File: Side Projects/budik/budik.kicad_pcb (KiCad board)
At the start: 2 copper layers, 122 x 65 mm, 92 parts, among them J1 Conn_01x02_Male, J2 USB_OTG, J3 FTDI, Q1 BSS138, SW1 SW_DPST, SW2 SW_DPST, SW3 SW_SPDT, SW4 SW_DPST, SW5 SW_DPST, U1 ESP-12, U2 MCP23018-E_SP, U3 uA7805, U4 LD1117S33CTR

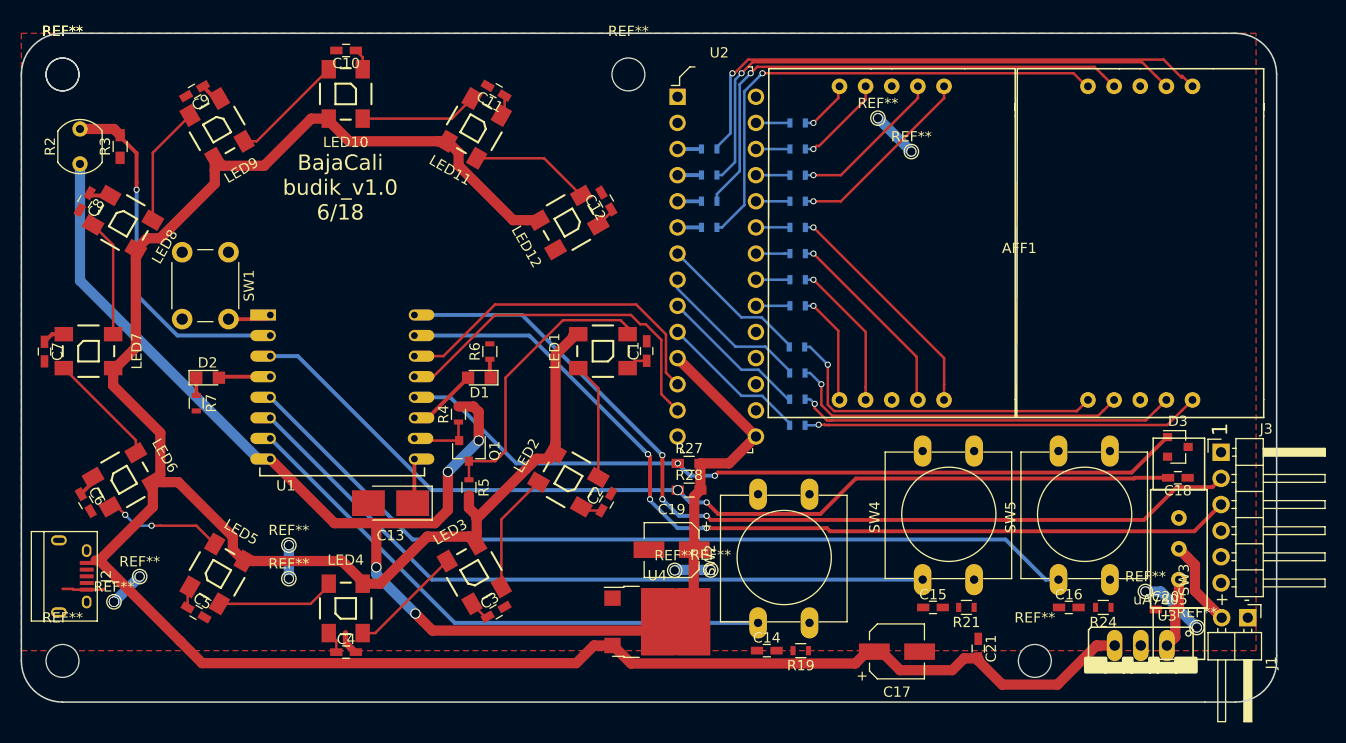
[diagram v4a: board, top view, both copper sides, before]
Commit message: Remake PCB into something like square
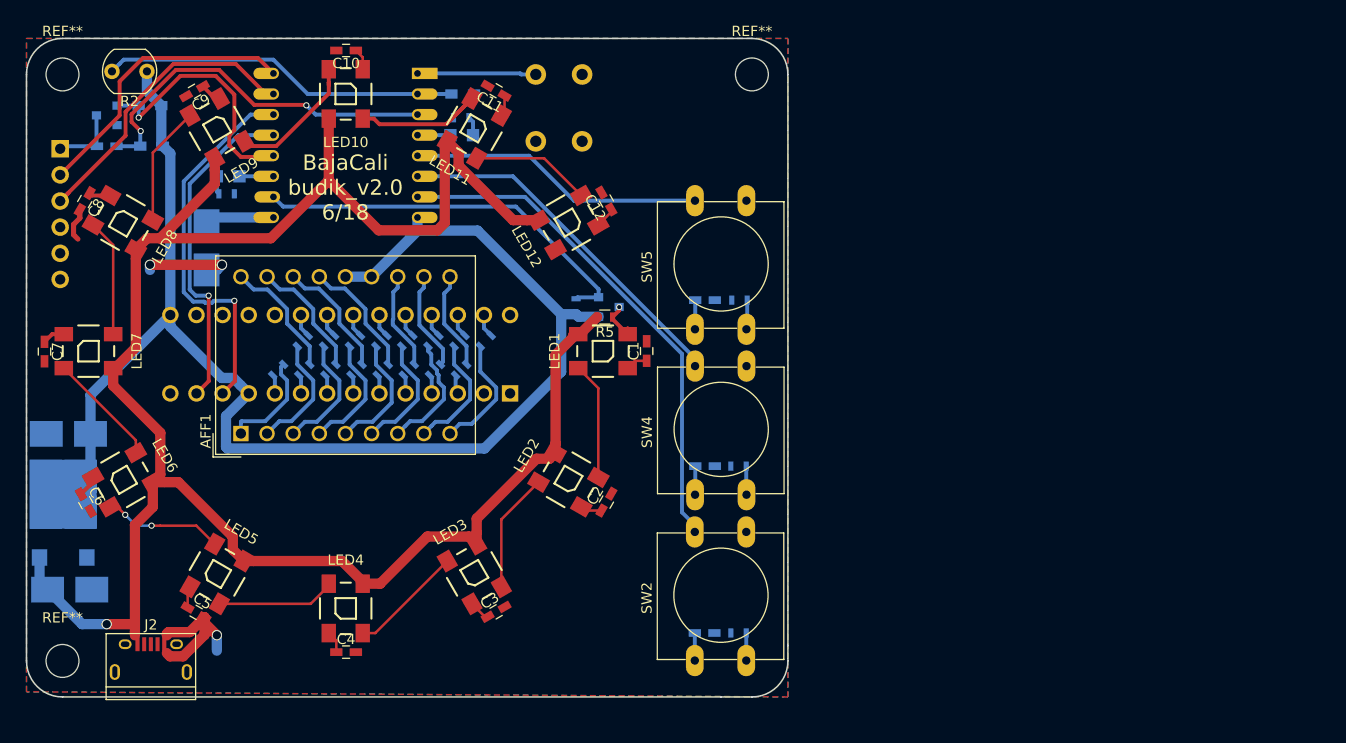
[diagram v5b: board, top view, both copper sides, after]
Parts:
- removed C20: 0.33u, Capacitors_SMD:C_0603_HandSoldering
- removed C21: 0.1u, Capacitors_SMD:C_0603_HandSoldering
- removed J1: Conn_01x02_Male, Pin_Headers:Pin_Header_Angled_1x02_Pitch2.54mm
- removed the REF** at (87.0, 112.2)
- removed the REF** at (118.5, 121.0)
- removed the REF** at (24.0, 64.0)
- removed the REF** at (79.0, 64.0)
- removed the REF** at (31.5, 112.8)
- removed the REF** at (103.2, 68.2)
- removed the REF** at (106.5, 71.5)
- removed the REF** at (134.2, 117.8)
- removed the REF** at (129.2, 114.2)
- removed the REF** at (83.5, 112.2)
- removed the REF** at (46.0, 113.0)
- removed the REF** at (46.0, 109.8)
- removed the REF** at (29.0, 115.2)
- removed SW3: SW_SPDT, 7_segment:switch
- removed U3: uA7805, L7805:78XXS
- added REF**: MountingHole_3.2mm_M3, Mounting_Holes:MountingHole_3.2mm_M3, F.Cu at (91.0, 64.0)
- AFF1: footprint 7_segment:7segment_double -> Displays_7-Segment:DA56-11CGKWA
- C13, C14, C15, C16, C18, D1, D2, D3, J3, Q1, R19, R21, R24, R27, R28, R3, R4, R6, R7, SW1, U1, U2, U4: moved to B.Cu
- C17: value 100n -> 10u; footprint Capacitors_SMD:CP_Elec_5x5.3 -> Capacitors_Tantalum_SMD:CP_Tantalum_Case-B_EIA-3528-21_Hand; moved to B.Cu
- C19: footprint Capacitors_SMD:CP_Elec_5x5.3 -> Capacitors_Tantalum_SMD:CP_Tantalum_Case-B_EIA-3528-21_Hand; moved to B.Cu
- moved J3 116.6 mm to (23.8, 71.2), turned to 180 degrees
- moved C18 109.0 mm to (28.3, 71.0), turned to 0 degrees
- moved D3 109.0 mm to (28.3, 68.0), turned to 180 degrees
- moved C17 80.6 mm to (24.7, 114.1)
- moved AFF1 77.7 mm to (41.3, 98.9), turned to 90 degrees
- moved R27 62.9 mm to (32.5, 67.0)
- moved R28 62.0 mm to (32.7, 71.0)
- moved C19 59.7 mm to (24.6, 98.9)
- moved U4 58.7 mm to (24.1, 106.6), turned to 90 degrees
- moved R8 52.6 mm to (47.4, 89.9), turned to 45 degrees
- moved R17 50.7 mm to (45.0, 92.7), turned to 225 degrees
- moved R9 48.0 mm to (47.5, 92.7), turned to 225 degrees
- moved R24 46.3 mm to (89.8, 85.9)
- moved C16 46.3 mm to (86.4, 85.9)
- moved R18 45.9 mm to (52.4, 89.9), turned to 45 degrees
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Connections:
- AFF1 pad 17: GND -> +3V3
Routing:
- net +5V: track 263.8 -> 194.5 mm, vias 0 -> 1
- net TX: track 90.8 -> 28.8 mm, vias 3 -> 0
- net RX: track 89.9 -> 30.0 mm, vias 3 -> 0
- net CH_PD: track 95.1 -> 37.2 mm
- net GPIO0: track 77.9 -> 25.0 mm, vias 2 -> 1
- net Bt3: track 84.1 -> 31.6 mm
- net Net-(AFF1-Pad12): track 54.5 -> 9.65 mm, vias 1 -> 0
- net Net-(AFF1-Pad10): track 53.9 -> 9.75 mm, vias 1 -> 0
- net Net-(AFF1-Pad11): track 50.4 -> 9.58 mm, vias 1 -> 0
- net Net-(AFF1-Pad9): track 49.3 -> 12.1 mm, vias 1 -> 0
- net Bt2: track 70.1 -> 37.8 mm
- net DATA_LED: track 6.27 -> 38.4 mm
- net Net-(AFF1-Pad5): track 39.0 -> 10.3 mm, vias 1 -> 0
- net Net-(AFF1-Pad8): track 37.6 -> 12.1 mm, vias 1 -> 0
- net DATA_LED_5V: track 28.0 -> 4.17 mm, vias 0 -> 1
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- added copper zone on B.Cu, net GND
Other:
- board size 122 x 65 mm -> 74 x 64 mm
- board text added: "BajaCali budik_v2.0 6/18"
- board text removed: "+"
- board text removed: "-"
- board text removed: "BajaCali budik_v1.0 6/18"

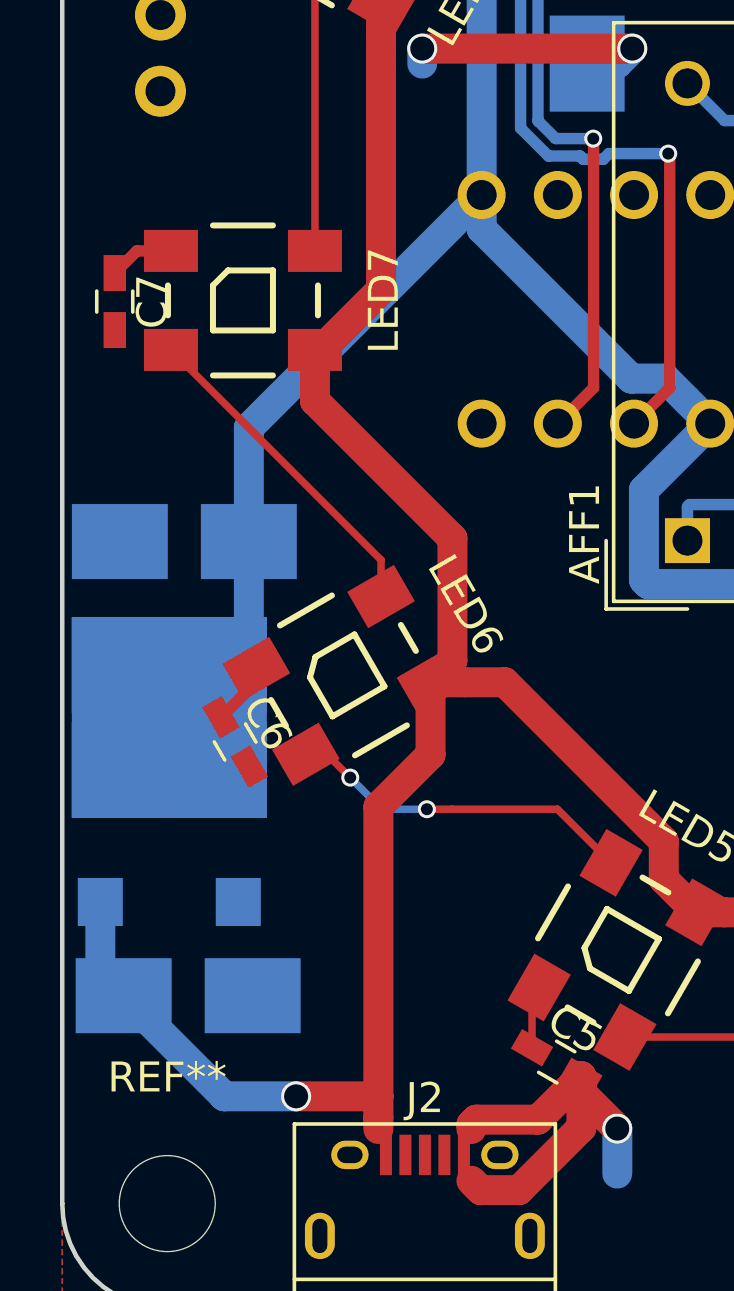
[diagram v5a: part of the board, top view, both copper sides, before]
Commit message: Move voltage regulator further from the board margin
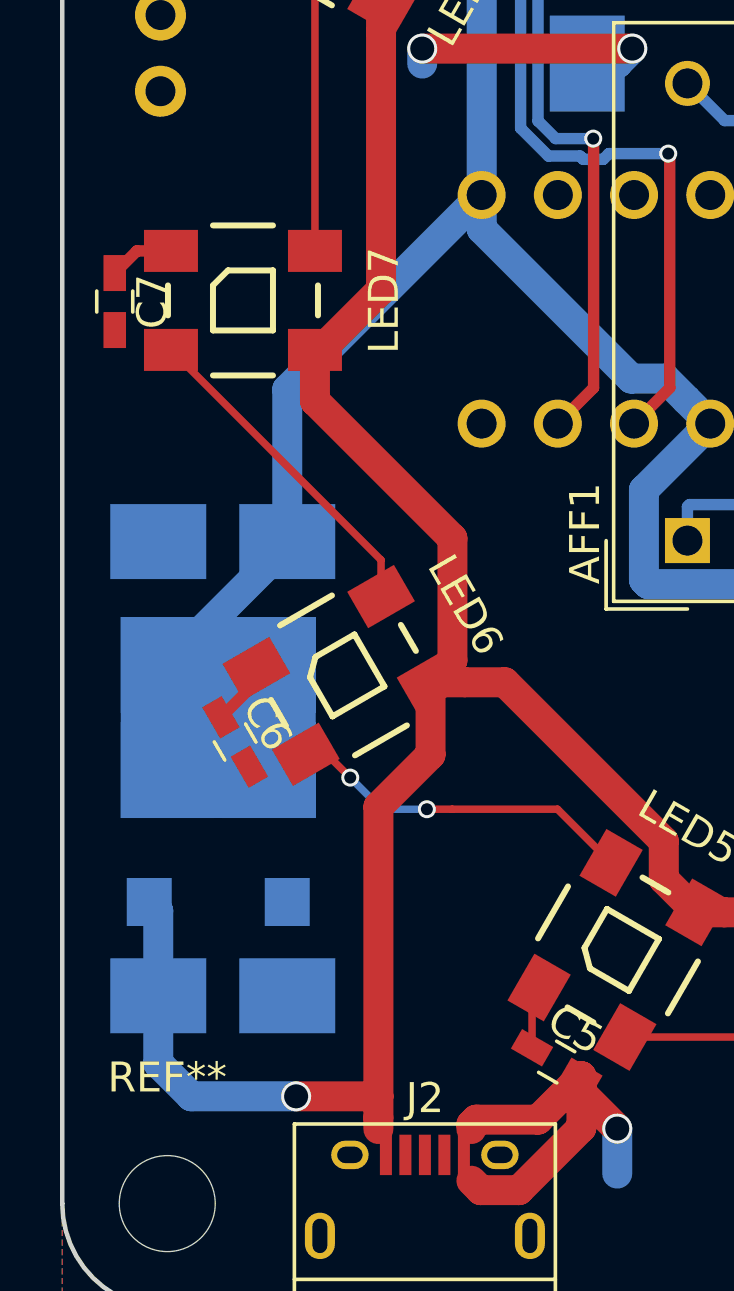
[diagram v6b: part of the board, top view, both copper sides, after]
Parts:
- moved U4 1.63 mm to (25.7, 106.6)
- moved C19 1.28 mm to (25.9, 98.9)
- moved C17 1.15 mm to (25.9, 114.1)
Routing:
- net +3V3: track 134.0 -> 136.1 mm
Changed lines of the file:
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@@
-(kicad_pcb (version 4) (host pcbnew 4.0.7)
+(kicad_pcb (version 4) (host pcbnew 4.0.7+dfsg1-1ubuntu2)
   (general
     (links 156)
-    (no_connects 15)
+    (no_connects 14)
     (area 20.424999 60.424999 94.575001 124.575001)
     (thickness 1.6)
     (drawings 12)
-    (tracks 459)
+    (tracks 462)
     (zones 0)
     (modules 75)
@@
   )
   (setup
-    (last_trace_width 0.381)
+    (last_trace_width 1)
     (user_trace_width 0.381)
     (user_trace_width 0.5)
@@
     (visible_elements FFFFFF7F)
     (pcbplotparams
-      (layerselection 0x00030_80000001)
+      (layerselection 0x000f0_80000001)
       (usegerberextensions false)
       (excludeedgelayer true)
@@
       (outputformat 1)
       (mirror false)
-      (drillshape 1)
+      (drillshape 0)
       (scaleselection 1)
-      (outputdirectory ""))
+      (outputdirectory gerber))
   )
   (net 0 "")
@@
   )
   (module TO_SOT_Packages_SMD:ATPAK-2 (layer B.Cu)
-    (at 24.0678 106.5972 90)
+    (at 25.7 106.5972 90)
     (descr "ATPAK SMD package, http://www.onsemi.com/pub/Collateral/ENA2192-D.PDF")
     (tags "ATPAK ")
@@
   )
   (module Capacitors_Tantalum_SMD:CP_Tantalum_Case-B_EIA-3528-21_Hand (layer B.Cu)
-    (at 24.6978 114.0714)
+    (at 25.85 114.0714)
     (descr "Tantalum capacitor, Case B, EIA 3528-21, 3.5x2.8x1.9mm, Hand soldering footprint")
     (tags "capacitor tantalum smd")
@@
   )
   (module Capacitors_Tantalum_SMD:CP_Tantalum_Case-B_EIA-3528-21_Hand (layer B.Cu)
-    (at 24.5708 98.933 180)
+    (at 25.85 98.933 180)
     (descr "Tantalum capacitor, Case B, EIA 3528-21, 3.5x2.8x1.9mm, Hand soldering footprint")
     (tags "capacitor tantalum smd")
@@
   (segment (start 44.5 77.9) (end 38.8 77.9) (width 1) (layer B.Cu) (net 24))
   (segment (start 38.8 77.9) (end 38 78.7) (width 1) (layer B.Cu) (net 24))
+  (segment (start 23.7 114.0714) (end 23.7 111.2472) (width 1) (layer B.Cu) (net 25))
+  (segment (start 23.7 111.2472) (end 23.4 110.9472) (width 1) (layer B.Cu) (net 25))
+  (segment (start 28.2956 117.4242) (end 24.8028 117.4242) (width 1) (layer B.Cu) (net 25))
+  (segment (start 24.8028 117.4242) (end 23.7 116.3214) (width 1) (layer B.Cu) (net 25))
+  (segment (start 23.7 116.3214) (end 23.7 114.0714) (width 1) (layer B.Cu) (net 25))
   (segment (start 61.395057 70.496825) (end 61.15001 70.741872) (width 1) (layer F.Cu) (net 25))
   (segment (start 61.15001 70.741872) (end 61.15001 78.417771) (width 1) (layer F.Cu) (net 25))
@@
   (segment (start 74.124 89.244) (end 74.2932 89.244) (width 1) (layer F.Cu) (net 25))
   (segment (start 74.2932 89.244) (end 75.958 87.5792) (width 1) (layer F.Cu) (net 25))
-  (segment (start 28.2956 117.4242) (end 25.9006 117.4242) (width 1) (layer B.Cu) (net 25))
-  (segment (start 25.9006 117.4242) (end 22.5478 114.0714) (width 1) (layer B.Cu) (net 25))
   (segment (start 31.038199 117.4242) (end 31.038199 118.141199) (width 1) (layer F.Cu) (net 25))
   (segment (start 31.038199 107.772801) (end 31.038199 117.4242) (width 1) (layer F.Cu) (net 25))
   (segment (start 31.038199 117.4242) (end 28.2956 117.4242) (width 1) (layer F.Cu) (net 25))
   (via (at 28.2956 117.4242) (size 1) (drill 0.8) (layers F.Cu B.Cu) (net 25))
-  (segment (start 21.7678 110.9472) (end 21.7678 113.2914) (width 1) (layer B.Cu) (net 25))
-  (segment (start 21.7678 113.2914) (end 22.5478 114.0714) (width 1) (layer B.Cu) (net 25))
   (segment (start 31.038199 118.141199) (end 31.038199 118.514484) (width 1) (layer F.Cu) (net 25))
   (segment (start 32.776825 106.034175) (end 31.038199 107.772801) (width 1) (layer F.Cu) (net 25))
@@
   (segment (start 29.25127 70.97838) (end 31.54582 70.97838) (width 0.381) (layer B.Cu) (net 26))
   (segment (start 31.54582 70.97838) (end 31.5566 70.9676) (width 0.381) (layer B.Cu) (net 26))
+  (segment (start 28 98.933) (end 28 93.86) (width 1) (layer B.Cu) (net 27))
+  (segment (start 28 93.86) (end 34.48 87.38) (width 1) (layer B.Cu) (net 27))
+  (segment (start 34.48 87.38) (end 34.43489 87.38) (width 1) (layer B.Cu) (net 27))
+  (segment (start 28 98.933) (end 28 99.0472) (width 1) (layer B.Cu) (net 27))
+  (segment (start 28 99.0472) (end 24 103.0472) (width 1) (layer B.Cu) (net 27))
   (segment (start 76.1 87.55) (end 74.1628 87.55) (width 1) (layer B.Cu) (net 27))
   (segment (start 74.1628 87.55) (end 73.914 87.3012) (width 1) (layer B.Cu) (net 27))
@@
   (segment (start 58.5 77.9) (end 58.5 79.1568) (width 1) (layer B.Cu) (net 27))
   (segment (start 58.5 79.1568) (end 58.5216 79.1784) (width 1) (layer B.Cu) (net 27))
-  (segment (start 26.7208 98.933) (end 26.7208 102.0942) (width 1) (layer B.Cu) (net 27))
   (segment (start 26.7208 102.0942) (end 25.7678 103.0472) (width 1) (layer B.Cu) (net 27))
-  (segment (start 34.48 87.38) (end 26.7208 95.1392) (width 1) (layer B.Cu) (net 27))
-  (segment (start 26.7208 95.1392) (end 26.7208 98.933) (width 1) (layer B.Cu) (net 27))
   (segment (start 34.48 87.38) (end 34.48 88.51137) (width 1) (layer B.Cu) (net 27))
   (segment (start 34.48 88.51137) (end 39.468629 93.499999) (width 1) (layer B.Cu) (net 27))
